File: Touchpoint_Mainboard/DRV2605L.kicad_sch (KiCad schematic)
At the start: 6 parts, among them U7 DRV2605LDGS

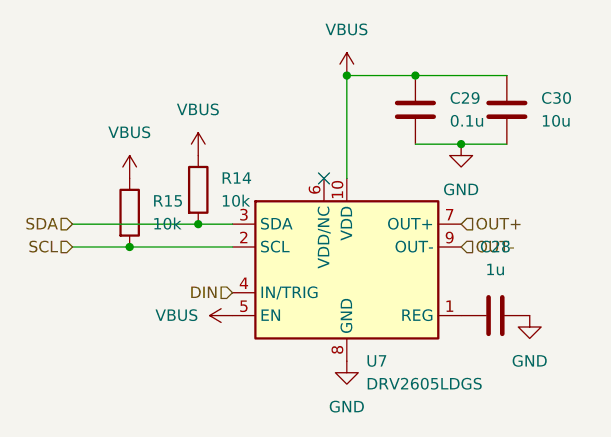
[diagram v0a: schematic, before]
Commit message: FInished populating mainboard schematic
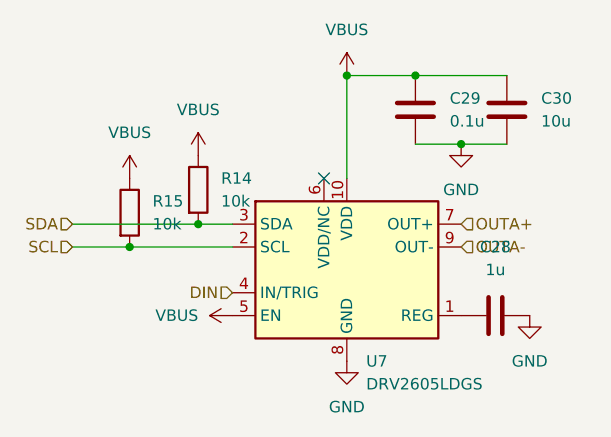
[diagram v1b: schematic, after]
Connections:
- net OUT+ renamed OUTA+
- net OUT- renamed OUTA-
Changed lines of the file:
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@@
 		)
 	)
-	(hierarchical_label "OUT+"
+	(hierarchical_label "OUTA+"
 		(shape input)
 		(at 72.39 45.72 0)
@@
 		)
 	)
-	(hierarchical_label "OUT-"
+	(hierarchical_label "OUTA-"
 		(shape input)
 		(at 72.39 48.26 0)

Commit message: Finished assigning most footprints
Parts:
- C28, C29: footprint (none) -> Capacitor_SMD:C_0402_1005Metric
- C30: footprint (none) -> Capacitor_SMD:C_0805_2012Metric
- R14, R15: footprint (none) -> Resistor_SMD:R_0402_1005Metric
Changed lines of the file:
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@@
 			)
 		)
-		(property "Footprint" ""
+		(property "Footprint" "Resistor_SMD:R_0402_1005Metric"
 			(at 33.782 44.45 90)
 			(effects
@@
 			)
 		)
-		(property "Footprint" ""
+		(property "Footprint" "Capacitor_SMD:C_0402_1005Metric"
 			(at 80.01 54.9148 0)
 			(effects
@@
 			)
 		)
-		(property "Footprint" ""
+		(property "Footprint" "Capacitor_SMD:C_0402_1005Metric"
 			(at 68.2752 36.83 0)
 			(effects
@@
 			)
 		)
-		(property "Footprint" ""
+		(property "Footprint" "Capacitor_SMD:C_0805_2012Metric"
 			(at 78.4352 36.83 0)
 			(effects
@@
 			)
 		)
-		(property "Footprint" ""
+		(property "Footprint" "Resistor_SMD:R_0402_1005Metric"
 			(at 41.402 41.91 90)
 			(effects

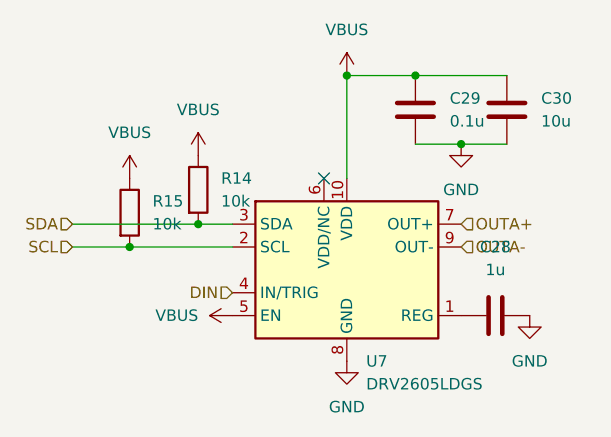
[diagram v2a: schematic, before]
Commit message: Added 3.3V to interface
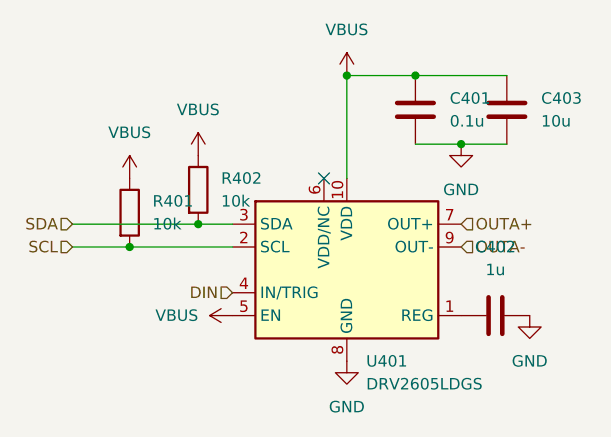
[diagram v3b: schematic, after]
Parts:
- renumbered C29 to C401, C28 to C402, C30 to C403, R15 to R401, R14 to R402, U7 to U401
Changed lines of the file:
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@@
 		(dnp no)
 		(fields_autoplaced yes)
-		(property "Reference" "#PWR044"
+		(property "Reference" "#PWR0405"
 			(at 59.69 67.31 0)
 			(effects
@@
 			(project ""
 				(path "/f37b5f88-420a-4646-85df-8f9851d23e3c/aa39997b-4c0a-48ee-8ceb-f8179578d7b0"
-					(reference "#PWR044")
+					(reference "#PWR0405")
 					(unit 1)
 				)
@@
 		(dnp no)
 		(fields_autoplaced yes)
-		(property "Reference" "#PWR042"
+		(property "Reference" "#PWR0402"
 			(at 43.18 41.91 0)
 			(effects
@@
 			(project ""
 				(path "/f37b5f88-420a-4646-85df-8f9851d23e3c/aa39997b-4c0a-48ee-8ceb-f8179578d7b0"
-					(reference "#PWR042")
+					(reference "#PWR0402")
 					(unit 1)
 				)
@@
 		(dnp no)
 		(fields_autoplaced yes)
-		(property "Reference" "R15"
+		(property "Reference" "R401"
 			(at 38.1 43.1799 0)
 			(effects
@@
 			(project "Touchpoint_Mainboard"
 				(path "/f37b5f88-420a-4646-85df-8f9851d23e3c/aa39997b-4c0a-48ee-8ceb-f8179578d7b0"
-					(reference "R15")
+					(reference "R401")
 					(unit 1)
 				)
@@
 		(dnp no)
 		(fields_autoplaced yes)
-		(property "Reference" "C28"
+		(property "Reference" "C402"
 			(at 76.2 48.26 90)
 			(effects
@@
 			(project ""
 				(path "/f37b5f88-420a-4646-85df-8f9851d23e3c/aa39997b-4c0a-48ee-8ceb-f8179578d7b0"
-					(reference "C28")
+					(reference "C402")
 					(unit 1)
 				)
@@
 		(dnp no)
 		(fields_autoplaced yes)
-		(property "Reference" "#PWR046"
+		(property "Reference" "#PWR0404"
 			(at 59.69 33.02 0)
 			(effects
@@
 			(project "Touchpoint_Mainboard"
 				(path "/f37b5f88-420a-4646-85df-8f9851d23e3c/aa39997b-4c0a-48ee-8ceb-f8179578d7b0"
-					(reference "#PWR046")
+					(reference "#PWR0404")
 					(unit 1)
 				)
@@
 		(dnp no)
 		(fields_autoplaced yes)
-		(property "Reference" "#PWR043"
+		(property "Reference" "#PWR0401"
 			(at 35.56 44.45 0)
 			(effects
@@
 			(project "Touchpoint_Mainboard"
 				(path "/f37b5f88-420a-4646-85df-8f9851d23e3c/aa39997b-4c0a-48ee-8ceb-f8179578d7b0"
-					(reference "#PWR043")
+					(reference "#PWR0401")
 					(unit 1)
 				)
@@
 		(dnp no)
 		(fields_autoplaced yes)
-		(property "Reference" "#PWR047"
+		(property "Reference" "#PWR0406"
 			(at 72.39 43.18 0)
 			(effects
@@
 			(project "Touchpoint_Mainboard"
 				(path "/f37b5f88-420a-4646-85df-8f9851d23e3c/aa39997b-4c0a-48ee-8ceb-f8179578d7b0"
-					(reference "#PWR047")
+					(reference "#PWR0406")
 					(unit 1)
 				)
@@
 		(dnp no)
 		(fields_autoplaced yes)
-		(property "Reference" "C29"
+		(property "Reference" "C401"
 			(at 71.12 31.7499 0)
 			(effects
@@
 			(project "Touchpoint_Mainboard"
 				(path "/f37b5f88-420a-4646-85df-8f9851d23e3c/aa39997b-4c0a-48ee-8ceb-f8179578d7b0"
-					(reference "C29")
+					(reference "C401")
 					(unit 1)
 				)
@@
 		(dnp no)
 		(fields_autoplaced yes)
-		(property "Reference" "#PWR048"
+		(property "Reference" "#PWR0403"
 			(at 50.8 55.88 0)
 			(effects
@@
 			(project "Touchpoint_Mainboard"
 				(path "/f37b5f88-420a-4646-85df-8f9851d23e3c/aa39997b-4c0a-48ee-8ceb-f8179578d7b0"
-					(reference "#PWR048")
+					(reference "#PWR0403")
 					(unit 1)
 				)
@@
 		(dnp no)
 		(fields_autoplaced yes)
-		(property "Reference" "#PWR045"
+		(property "Reference" "#PWR0407"
 			(at 80.01 62.23 0)
 			(effects
@@
 			(project "Touchpoint_Mainboard"
 				(path "/f37b5f88-420a-4646-85df-8f9851d23e3c/aa39997b-4c0a-48ee-8ceb-f8179578d7b0"
-					(reference "#PWR045")
+					(reference "#PWR0407")
 					(unit 1)
 				)
@@
 		(dnp no)
 		(fields_autoplaced yes)
-		(property "Reference" "U7"
+		(property "Reference" "U401"
 			(at 61.8333 60.96 0)
 			(effects
@@
 			(project ""
 				(path "/f37b5f88-420a-4646-85df-8f9851d23e3c/aa39997b-4c0a-48ee-8ceb-f8179578d7b0"
-					(reference "U7")
+					(reference "U401")
 					(unit 1)
 				)
@@
 		(dnp no)
 		(fields_autoplaced yes)
-		(property "Reference" "C30"
+		(property "Reference" "C403"
 			(at 81.28 31.7499 0)
 			(effects
@@
 			(project "Touchpoint_Mainboard"
 				(path "/f37b5f88-420a-4646-85df-8f9851d23e3c/aa39997b-4c0a-48ee-8ceb-f8179578d7b0"
-					(reference "C30")
+					(reference "C403")
 					(unit 1)
 				)
@@
 		(dnp no)
 		(fields_autoplaced yes)
-		(property "Reference" "R14"
+		(property "Reference" "R402"
 			(at 45.72 40.6399 0)
 			(effects
@@
 			(project ""
 				(path "/f37b5f88-420a-4646-85df-8f9851d23e3c/aa39997b-4c0a-48ee-8ceb-f8179578d7b0"
-					(reference "R14")
-					(unit 1)
-				)
+					(reference "R402")
+					(unit 1)
+				)

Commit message: Finally finished routing EEOP driver
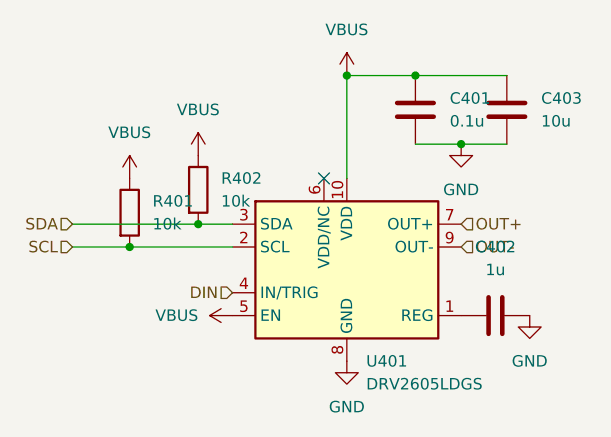
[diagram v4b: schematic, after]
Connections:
- net OUTA+ renamed OUT+
- net OUTA- renamed OUT-
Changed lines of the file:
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@@
 		)
 	)
-	(hierarchical_label "OUTA+"
+	(hierarchical_label "OUT+"
 		(shape input)
 		(at 72.39 45.72 0)
@@
 		)
 	)
-	(hierarchical_label "OUTA-"
+	(hierarchical_label "OUT-"
 		(shape input)
 		(at 72.39 48.26 0)
